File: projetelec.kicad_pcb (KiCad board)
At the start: 2 copper layers, 91 x 113.5 mm, 54 parts, among them J1 PINHD_1x2_Male, J2 PINHD_1x15_Female, J3 PINHD_1x15_Female, Q1 2N7000, U1 NE555P

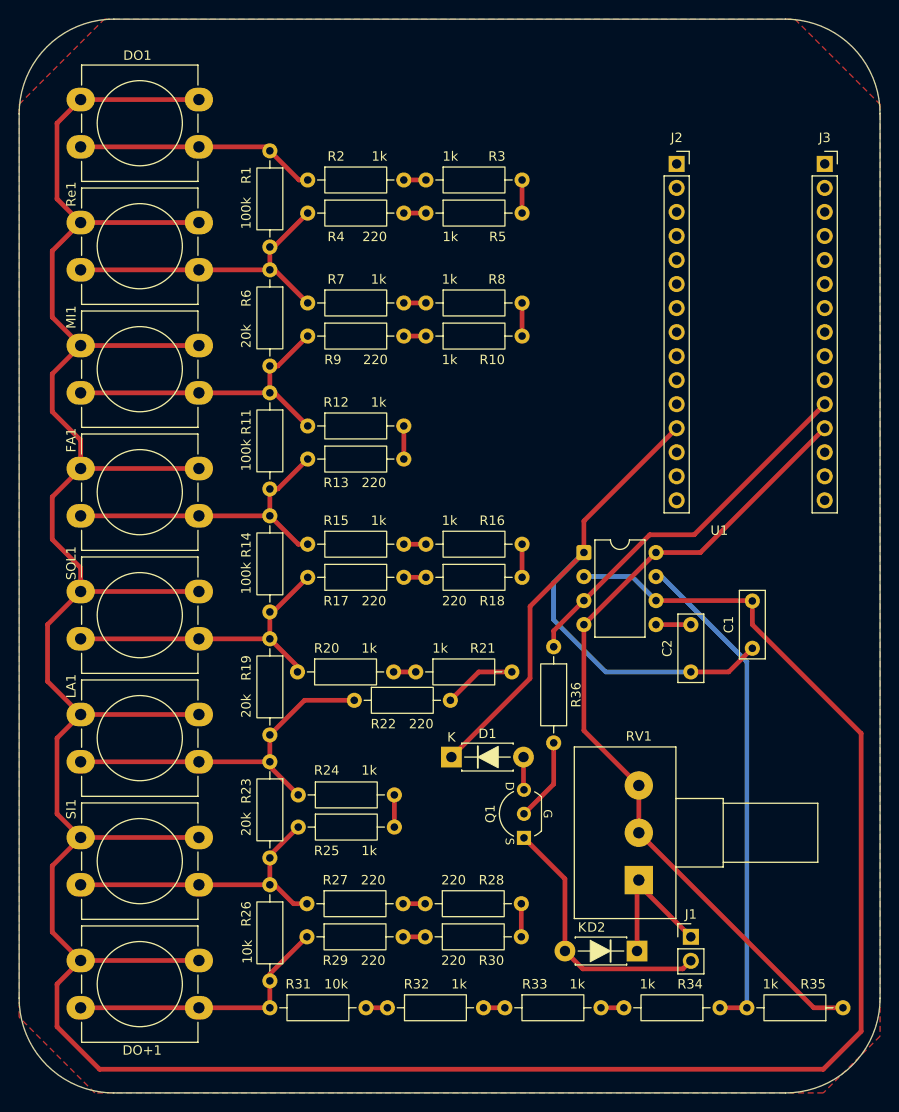
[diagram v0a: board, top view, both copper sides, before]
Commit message: Add freerouting.dsn; update KiCad files & backups
Add FreeRouting session file (freerouting.dsn) and a temporary freerouting export (temp-freerouting.dsn). Remove outdated freerouting.rules and several old projetelec backup ZIPs, and add new backup ZIPs (2026-04-07 through 2026-04-09). Update KiCad project files (projetelec.kicad_pcb, projetelec.kicad_prl, projetelec.kicad_pro, projetelec.kicad_sch) and add projetelectest project files. These changes integrate a freerouter export and refresh project metadata and backups.
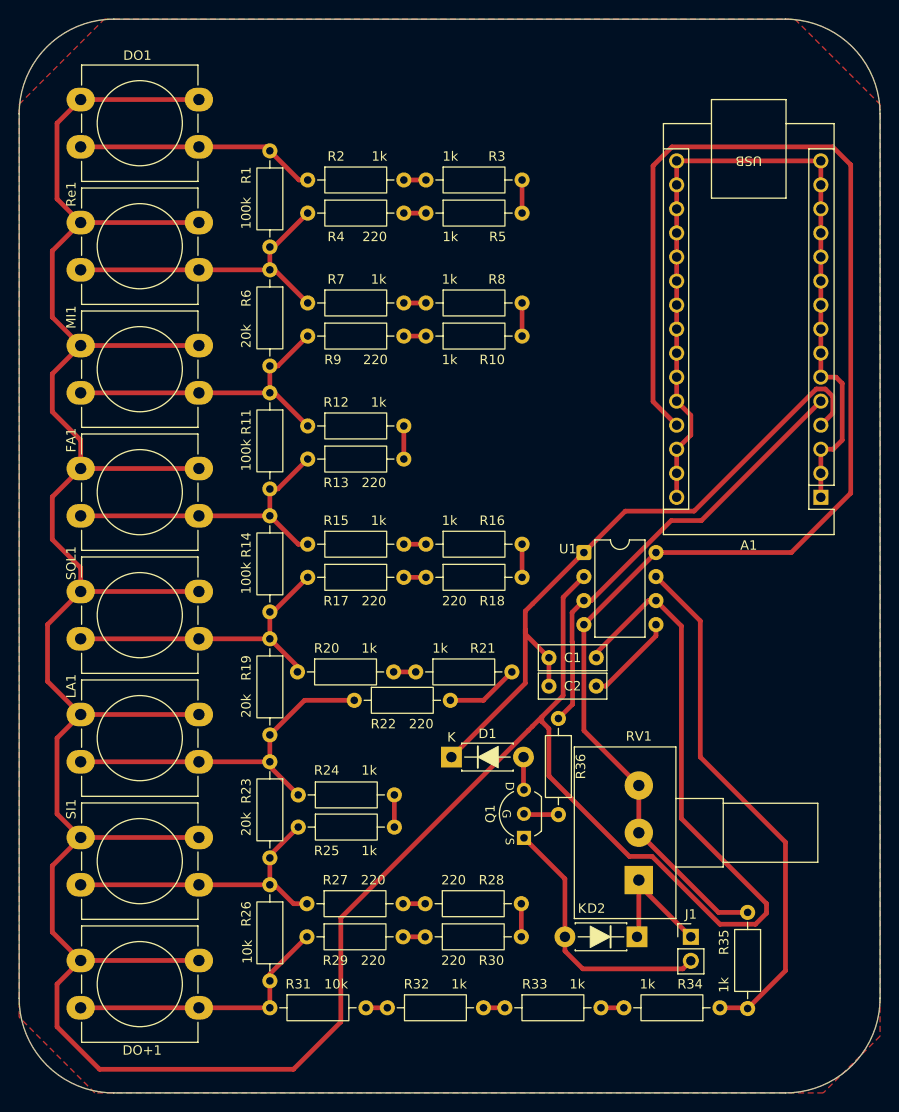
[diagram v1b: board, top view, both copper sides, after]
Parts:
- removed J2, J3: PINHD_1x15_Female, Connector_PinSocket_2.54mm:PinSocket_1x15_P2.54mm_Vertical
- added A1: Arduino_Nano_v3.x, Module:Arduino_Nano, F.Cu at (109.7, 88.5)
- moved C1 21.5 mm to (81.0, 105.5), turned to 0 degrees
- moved C2 15.1 mm to (81.0, 108.5), turned to 0 degrees
- moved R35 14.3 mm to (102.0, 132.4), turned to -90 degrees
- moved R36 7.60 mm to (82.0, 111.9)
- moved D2 1.50 mm to (90.3, 135.0)
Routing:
- net Net-(A1-3V3): track 0.00 -> 91.2 mm
- net Net-(A1-+5V): track 87.7 -> 159.0 mm
- net Net-(U1-THRES): track 373.7 -> 391.2 mm
- net Net-(A1-D2): track 40.3 -> 47.4 mm
- net Net-(U1-CONT): track 3.69 -> 9.70 mm
- net Net-(D1-K): track 77.4 -> 71.8 mm
- net Net-(Q1-G): track 8.80 -> 3.67 mm
- net Net-(U1-DISCH): track 52.8 -> 55.8 mm
- net Net-(D2-K): track 15.9 -> 14.6 mm
- added copper zone on F.Cu, net (none)
- removed copper zone on F.Cu, net P,GND

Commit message: Update KiCad PCB format and nets
Add several backup archives and update KiCad project files. Bump projetelec.kicad_pcb version/generator_version and expand setup options (tenting/covering/plugging/capping/filling), normalize plot parameter formats, and remove explicit numbered net list entries in favor of named net references. Update many footprint entries (units, duplicate_pad_numbers_are_jumpers) and adjust pad net names, pin functions and component reference fixes to align with the new format. projetelec.kicad_prl, projetelec.kicad_pro and projetelec.kicad_sch were also modified to reflect these changes.
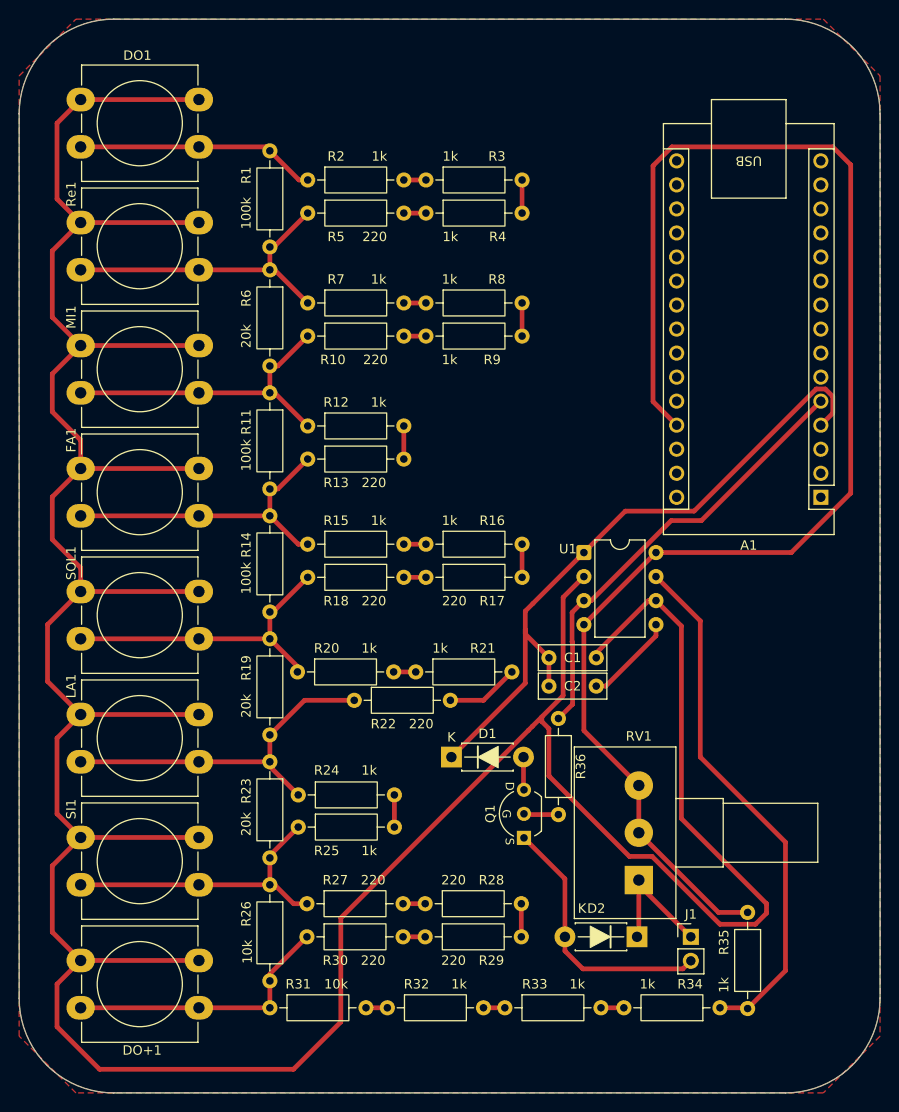
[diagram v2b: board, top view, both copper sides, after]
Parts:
- renumbered R9 to R10, R18 to R17, R17 to R18, R30 to R29, R29 to R30, R5 to R4, R4 to R5, R10 to R9
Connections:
- net Net-(A1-+5V) renamed 5V
- net Net-(A1-D2) renamed Pin 3
- net Net-(D1-K) renamed GND
- net Net-(U1-DISCH) renamed Pin 7
- net Net-(U1-THRES) renamed Pin 2 et 6
- A1 pad 1: Net-(A1-3V3) -> unconnected-(A1-D1/TX-Pad1)
- A1 pad 10: Net-(A1-3V3) -> unconnected-(A1-D7-Pad10)
- A1 pad 11: Net-(A1-3V3) -> unconnected-(A1-D8-Pad11)
- A1 pad 12: Net-(A1-3V3) -> unconnected-(A1-D9-Pad12)
- A1 pad 13: Net-(A1-3V3) -> unconnected-(A1-D10-Pad13)
- A1 pad 14: Net-(A1-3V3) -> unconnected-(A1-D11-Pad14)
- A1 pad 15: Net-(A1-3V3) -> unconnected-(A1-D12-Pad15)
- A1 pad 16: Net-(A1-3V3) -> unconnected-(A1-D13-Pad16)
- A1 pad 17: Net-(A1-3V3) -> unconnected-(A1-3V3-Pad17)
- A1 pad 18: Net-(A1-3V3) -> unconnected-(A1-AREF-Pad18)
- A1 pad 19: Net-(A1-3V3) -> unconnected-(A1-A0-Pad19)
- A1 pad 2: Net-(A1-3V3) -> unconnected-(A1-D0/RX-Pad2)
- A1 pad 20: Net-(A1-3V3) -> unconnected-(A1-A1-Pad20)
- A1 pad 21: Net-(A1-3V3) -> unconnected-(A1-A2-Pad21)
- A1 pad 22: Net-(A1-3V3) -> unconnected-(A1-A3-Pad22)
- A1 pad 23: Net-(A1-3V3) -> unconnected-(A1-A4-Pad23)
- A1 pad 24: Net-(A1-3V3) -> unconnected-(A1-A5-Pad24)
- A1 pad 25: Net-(A1-3V3) -> unconnected-(A1-A6-Pad25)
- A1 pad 26: Net-(A1-3V3) -> unconnected-(A1-A7-Pad26)
- A1 pad 28: Net-(A1-3V3) -> unconnected-(A1-~{RESET}-Pad28)
- A1 pad 29: Net-(A1-3V3) -> unconnected-(A1-GND-Pad29)
- A1 pad 3: Net-(A1-3V3) -> unconnected-(A1-~{RESET}-Pad3)
- A1 pad 30: Net-(A1-3V3) -> unconnected-(A1-VIN-Pad30)
- A1 pad 6: Net-(A1-3V3) -> unconnected-(A1-D3-Pad6)
- A1 pad 7: Net-(A1-3V3) -> unconnected-(A1-D4-Pad7)
- A1 pad 8: Net-(A1-3V3) -> unconnected-(A1-D5-Pad8)
- A1 pad 9: Net-(A1-3V3) -> unconnected-(A1-D6-Pad9)
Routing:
- net Net-(A1-3V3): track 91.2 -> 0.00 mm

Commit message: Add buzzer footprint and update PCB routing
Add three backup archives and introduce a new buzzer footprint (Buzzer_15x7.5RM7.6) with pads, silkscreen, properties and 3D model; bind the buzzer pad to the net "Buzzer". Update various footprint UUIDs, silkscreen/text positions and TO-92 orientation/labels, change a resistor value/placement, and perform extensive copper trace/segment and net adjustments (including changes to nets like "Pin 2 et 6" and "Net-(U1-CONT)") to reflect the revised layout.
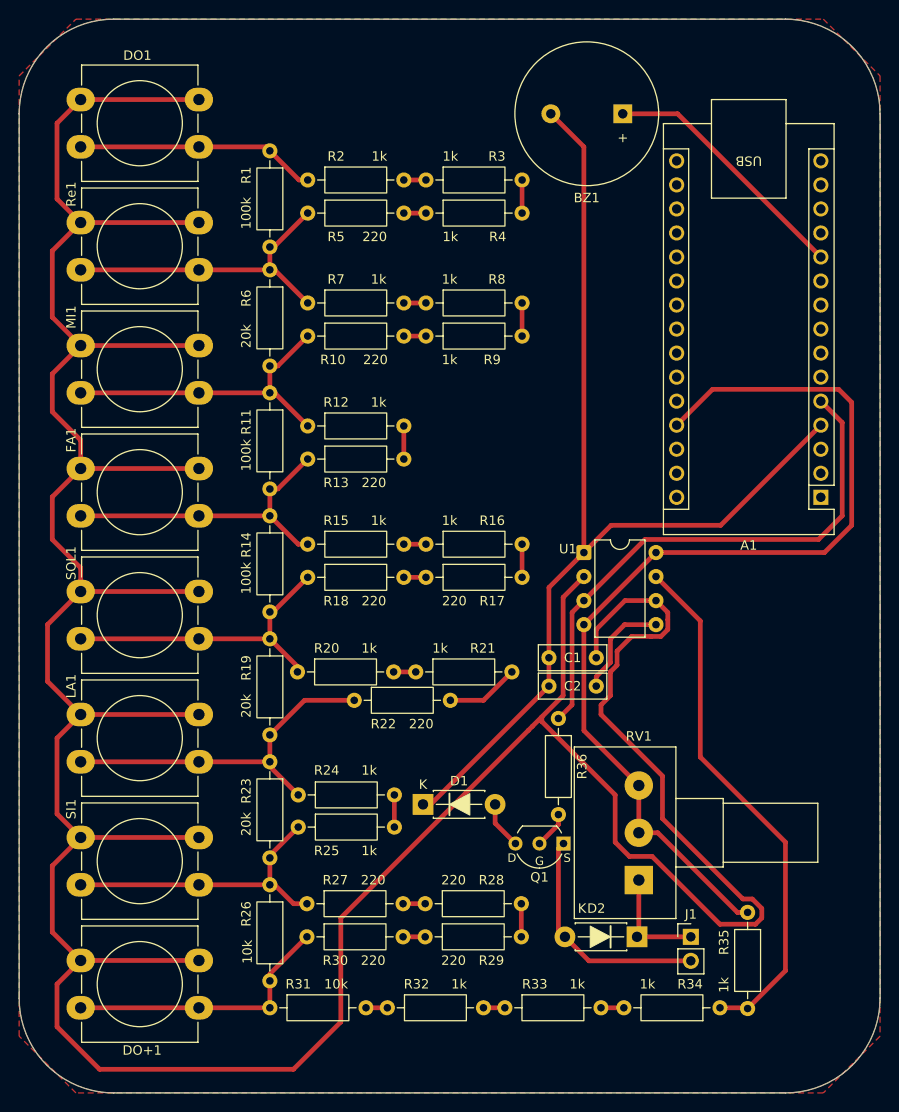
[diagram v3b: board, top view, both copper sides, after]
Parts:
- added BZ1: Buzzer, Buzzer_Beeper:Buzzer_15x7.5RM7.6, F.Cu at (88.8, 48.0)
- R36: value Resistor -> 1k
- moved D1 5.83 mm to (67.7, 121.0)
- moved Q1 4.22 mm to (82.5, 125.1), turned to 180 degrees
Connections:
- A1 pad 11: unconnected-(A1-D8-Pad11) -> Buzzer
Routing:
- net 5V: track 159.0 -> 105.7 mm
- net GND: track 71.8 -> 112.6 mm
- net Buzzer: track 0.00 -> 27.2 mm
- net Pin 3: track 47.4 -> 57.6 mm
- net Pin 2 et 6: track 391.2 -> 400.5 mm
- net Net-(D2-A): track 28.2 -> 24.7 mm
- net Net-(D2-K): track 14.6 -> 12.0 mm
- net Net-(D1-A): track 3.48 -> 5.03 mm
- net Net-(U1-CONT): track 9.70 -> 11.1 mm
- added copper zone on F.Cu, net GND
- removed copper zone on F.Cu, net (none)
